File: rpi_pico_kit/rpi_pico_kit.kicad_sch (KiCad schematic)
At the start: 34 parts, among them J1 DC Jack 5.5x2.1mm, J3 Conn_01x03_Male, Q1 DMN63D8L-7, Q2 DMN63D8L-7, SW1 SW_Push, U1 RPi Pico, U5 74HC14

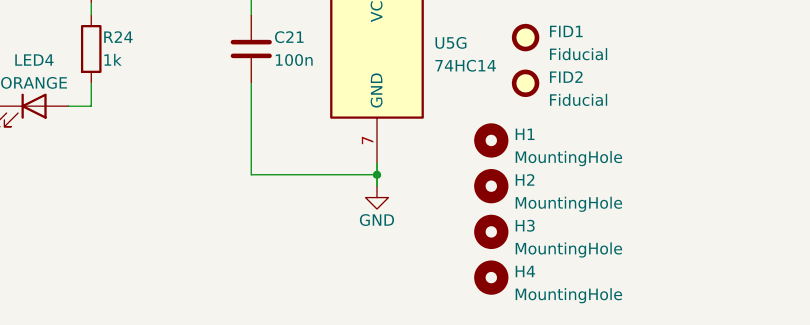
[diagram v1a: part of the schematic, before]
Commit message: added 5th hole at the center
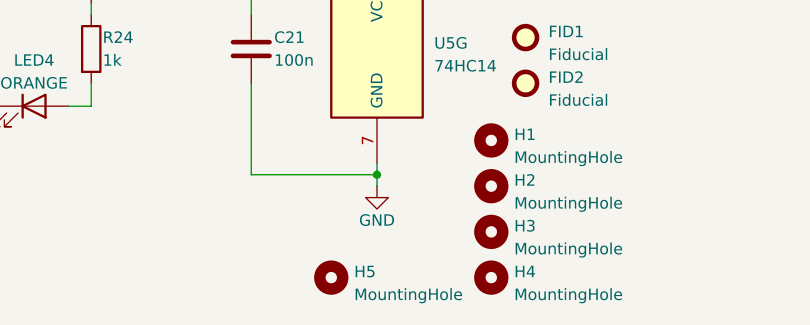
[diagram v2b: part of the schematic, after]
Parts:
- added H5: MountingHole, MountingHole:MountingHole_2.7mm_M2.5, symbol Mechanical:MountingHole
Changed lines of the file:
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@@
     (pin "2")
+  )
+  (symbol (lib_id "Mechanical:MountingHole") (at 142.24 194.31 0) (unit 1)
+    (in_bom yes) (on_board yes) (fields_autoplaced)
+    (property "Reference" "H5" (id 0) (at 144.78 193.675 0)
+      (effects (font (size 1.27 1.27)) (justify left))
+    )
+    (property "Value" "MountingHole" (id 1) (at 144.78 196.215 0)
+      (effects (font (size 1.27 1.27)) (justify left))
+    )
+    (property "Footprint" "MountingHole:MountingHole_2.7mm_M2.5" (id 2) (at 142.24 194.31 0)
+      (effects (font (size 1.27 1.27)) hide)
+    )
+    (property "Datasheet" "~" (id 3) (at 142.24 194.31 0)
+      (effects (font (size 1.27 1.27)) hide)
+    )
+    (property "Manufacturer Part Number" "~" (id 4) (at 142.24 194.31 0)
+      (effects (font (size 1.27 1.27)) hide)
+    )
+    (property "Supplier" "~" (id 5) (at 142.24 194.31 0)
+      (effects (font (size 1.27 1.27)) hide)
+    )
+    (property "Supplier Part URL" "~" (id 6) (at 142.24 194.31 0)
+      (effects (font (size 1.27 1.27)) hide)
+    )
   )
   (symbol (lib_id "power:GND") (at 85.09 158.75 0) (unit 1)
@@
       (reference "H4") (unit 1) (value "MountingHole") (footprint "MountingHole:MountingHole_2.7mm_M2.5")
     )
+    (path "/6a5cd9f1-fa39-4f86-88b6-0cd65263ec3f"
+      (reference "H5") (unit 1) (value "MountingHole") (footprint "MountingHole:MountingHole_2.7mm_M2.5")
+    )
     (path "/1be26fdf-4440-4eee-ae3b-ea83403c36c3"

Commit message: debugger (unrouted 163)
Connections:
- net +3V3: now also RN3.2 (R2.1), RN3.3 (R3.1); no longer RN3.1 (R1.1), RN3.2 (R2.1)
- net UART0_RX: now also RN3.7 (R2.2), RN3.8 (R1.2); no longer RN3.4 (R4.1), RN3.8 (R1.2)
- net UART0_TX: now also RN3.4 (R4.1); no longer RN3.3 (R3.1)
- net at U1.2 (GPIO1): now also RN3.1 (R1.1); no longer RN3.5 (R4.2)
- new net: RN3.5 (R4.2), RN3.6 (R3.2), U1.1 (GPIO0)
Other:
- moved on the sheet: RN3A
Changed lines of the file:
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@@
     (pin "1")
   )
-  (symbol (lib_id "Device:R_Pack04_Split") (at 44.45 36.83 270) (unit 4)
-    (in_bom yes) (on_board yes)
-    (property "Reference" "RN3" (id 0) (at 40.64 35.56 90)
+  (symbol (lib_id "Device:R_Pack04_Split") (at 44.45 36.83 90) (mirror x) (unit 1)
+    (in_bom yes) (on_board yes)
+    (property "Reference" "RN3" (id 0) (at 48.26 35.56 90)
       (effects (font (size 1.27 1.27)) (justify right))
     )
-    (property "Value" "1k" (id 1) (at 50.8 35.56 90)
+    (property "Value" "1k" (id 1) (at 38.1 35.56 90)
       (effects (font (size 1.27 1.27)) (justify right))
     )
@@
       (effects (font (size 1.27 1.27)) hide)
     )
-    (pin "4")
-    (pin "5")
+    (pin "1")
+    (pin "8")
   )
   (symbol (lib_id "power:GND") (at 140.97 62.23 0) (unit 1)
@@
     (pin "2")
   )
-  (symbol (lib_id "Device:R_Pack04_Split") (at 44.45 34.29 270) (unit 3)
+  (symbol (lib_id "Device:R_Pack04_Split") (at 44.45 34.29 270) (unit 4)
     (in_bom yes) (on_board yes)
     (property "Reference" "RN3" (id 0) (at 40.64 33.02 90)
@@
       (effects (font (size 1.27 1.27)) hide)
     )
-    (pin "3")
-    (pin "6")
+    (pin "4")
+    (pin "5")
   )
   (symbol (lib_id "Transistor_FET:BSS138") (at 144.78 101.6 270) (unit 1)
@@
     (pin "1")
   )
-  (symbol (lib_id "Device:R_Pack04_Split") (at 54.61 26.67 180) (unit 2)
+  (symbol (lib_id "Device:R_Pack04_Split") (at 54.61 26.67 180) (unit 3)
     (in_bom yes) (on_board yes)
     (property "Reference" "RN3" (id 0) (at 55.88 25.4 0)
@@
       (effects (font (size 1.27 1.27)) hide)
     )
-    (pin "2")
-    (pin "7")
+    (pin "3")
+    (pin "6")
   )
   (symbol (lib_id "power:GND") (at 196.85 151.13 90) (unit 1)
@@
     (pin "1")
   )
-  (symbol (lib_id "Device:R_Pack04_Split") (at 33.02 26.67 180) (unit 1)
+  (symbol (lib_id "Device:R_Pack04_Split") (at 33.02 26.67 180) (unit 2)
     (in_bom yes) (on_board yes)
     (property "Reference" "RN3" (id 0) (at 34.29 25.4 0)
@@
       (effects (font (size 1.27 1.27)) hide)
     )
-    (pin "1")
-    (pin "8")
+    (pin "2")
+    (pin "7")
   )
   (symbol (lib_id "Device:R") (at 115.57 140.97 0) (unit 1)
@@
       (reference "RN2") (unit 4) (value "270R") (footprint "Resistor_SMD:R_Array_Convex_4x0603")
     )
+    (path "/1ac4a7c2-b7be-4e1c-a497-ed6aab390c53"
+      (reference "RN3") (unit 1) (value "1k") (footprint "Resistor_SMD:R_Array_Convex_4x0603")
+    )
     (path "/d61b4a07-386e-408b-9033-b22a8b79e947"
-      (reference "RN3") (unit 1) (value "1k") (footprint "Resistor_SMD:R_Array_Convex_4x0603")
+      (reference "RN3") (unit 2) (value "1k") (footprint "Resistor_SMD:R_Array_Convex_4x0603")
     )
     (path "/cb5269f7-df36-404c-9295-80e9ad4fd32e"
-      (reference "RN3") (unit 2) (value "1k") (footprint "Resistor_SMD:R_Array_Convex_4x0603")
+      (reference "RN3") (unit 3) (value "1k") (footprint "Resistor_SMD:R_Array_Convex_4x0603")
     )
     (path "/5db5a00f-59fb-4bcf-a0f0-3bf8a625fc7d"
-      (reference "RN3") (unit 3) (value "1k") (footprint "Resistor_SMD:R_Array_Convex_4x0603")
-    )
-    (path "/1ac4a7c2-b7be-4e1c-a497-ed6aab390c53"
       (reference "RN3") (unit 4) (value "1k") (footprint "Resistor_SMD:R_Array_Convex_4x0603")
     )

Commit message: monostable (unrouted 136)
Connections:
- net UART0_RX: now also U5.3; no longer U5.5
- net at C19.2, R19.2, R20.1: now also U5.13; no longer U5.3
- net at LED3.1 (K): now also U5.12; no longer U5.4
- net at D5.2 (A): now also U5.4; no longer U5.6
- net at C20.2, R22.2, R23.1: now also U5.11; no longer U5.9
- net at LED4.1 (K): now also U5.10; no longer U5.8
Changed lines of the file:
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@@
     (pin "9")
   )
-  (symbol (lib_id "74xx:74HC14") (at 44.45 175.26 0) (unit 3)
+  (symbol (lib_id "74xx:74HC14") (at 44.45 175.26 0) (unit 2)
     (in_bom yes) (on_board yes) (fields_autoplaced)
     (property "Reference" "U5" (id 0) (at 44.45 167.64 0)
@@
       (effects (font (size 1.27 1.27)) hide)
     )
-    (pin "5")
-    (pin "6")
+    (pin "3")
+    (pin "4")
   )
   (symbol (lib_id "power:GND") (at 81.28 88.9 0) (unit 1)
@@
     (pin "1")
   )
-  (symbol (lib_id "74xx:74HC14") (at 95.25 175.26 0) (unit 4)
+  (symbol (lib_id "74xx:74HC14") (at 95.25 175.26 0) (unit 5)
     (in_bom yes) (on_board yes) (fields_autoplaced)
     (property "Reference" "U5" (id 0) (at 95.25 167.64 0)
@@
       (effects (font (size 1.27 1.27)) hide)
     )
-    (pin "8")
-    (pin "9")
+    (pin "10")
+    (pin "11")
   )
   (symbol (lib_id "power:GND") (at 74.93 158.75 0) (unit 1)
@@
     (pin "1")
   )
-  (symbol (lib_id "74xx:74HC14") (at 95.25 147.32 0) (unit 2)
+  (symbol (lib_id "74xx:74HC14") (at 95.25 147.32 0) (unit 6)
     (in_bom yes) (on_board yes) (fields_autoplaced)
     (property "Reference" "U5" (id 0) (at 95.25 139.7 0)
@@
       (effects (font (size 1.27 1.27)) hide)
     )
-    (pin "3")
-    (pin "4")
+    (pin "12")
+    (pin "13")
   )
   (symbol (lib_id "Device:R") (at 85.09 181.61 0) (unit 1)
@@
       (reference "U5") (unit 1) (value "74HC14") (footprint "Package_SO:SOIC-14_3.9x8.7mm_P1.27mm")
     )
+    (path "/919f662f-b70b-4993-9ea2-ad54dc351e72"
+      (reference "U5") (unit 2) (value "74HC14") (footprint "Package_SO:SOIC-14_3.9x8.7mm_P1.27mm")
+    )
+    (path "/fe15dc26-52fc-427e-8179-2b8bb41b57bb/f32a0f73-1820-4ea7-8063-dc0a550d2cec"
+      (reference "U5") (unit 3) (value "74HC14") (footprint "Package_SO:SOIC-14_3.9x8.7mm_P1.27mm")
+    )
+    (path "/fe15dc26-52fc-427e-8179-2b8bb41b57bb/bbbac723-7fcc-4a53-b5f6-de5daa58086a"
+      (reference "U5") (unit 4) (value "74HC14") (footprint "Package_SO:SOIC-14_3.9x8.7mm_P1.27mm")
+    )
+    (path "/d2118661-349f-4f17-a649-7ecad9caafc3"
+      (reference "U5") (unit 5) (value "74HC14") (footprint "Package_SO:SOIC-14_3.9x8.7mm_P1.27mm")
+    )
     (path "/f6bee219-67fb-464f-b724-02f155dc53f3"
-      (reference "U5") (unit 2) (value "74HC14") (footprint "Package_SO:SOIC-14_3.9x8.7mm_P1.27mm")
-    )
-    (path "/919f662f-b70b-4993-9ea2-ad54dc351e72"
-      (reference "U5") (unit 3) (value "74HC14") (footprint "Package_SO:SOIC-14_3.9x8.7mm_P1.27mm")
-    )
-    (path "/d2118661-349f-4f17-a649-7ecad9caafc3"
-      (reference "U5") (unit 4) (value "74HC14") (footprint "Package_SO:SOIC-14_3.9x8.7mm_P1.27mm")
-    )
-    (path "/fe15dc26-52fc-427e-8179-2b8bb41b57bb/f32a0f73-1820-4ea7-8063-dc0a550d2cec"
-      (reference "U5") (unit 5) (value "74HC14") (footprint "Package_SO:SOIC-14_3.9x8.7mm_P1.27mm")
-    )
-    (path "/fe15dc26-52fc-427e-8179-2b8bb41b57bb/bbbac723-7fcc-4a53-b5f6-de5daa58086a"
       (reference "U5") (unit 6) (value "74HC14") (footprint "Package_SO:SOIC-14_3.9x8.7mm_P1.27mm")
     )

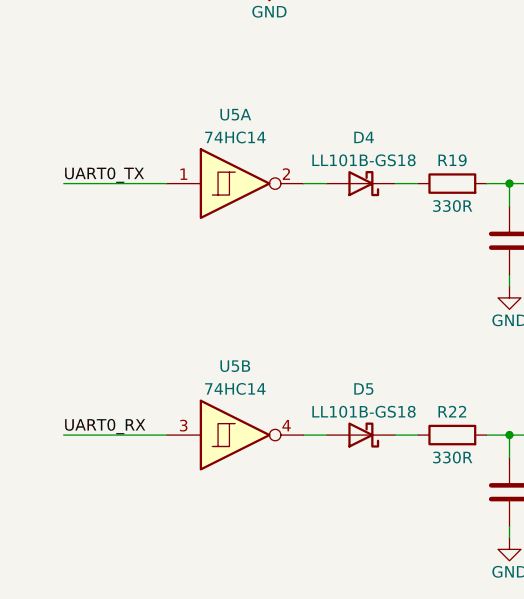
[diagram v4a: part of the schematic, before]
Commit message: changed pinout
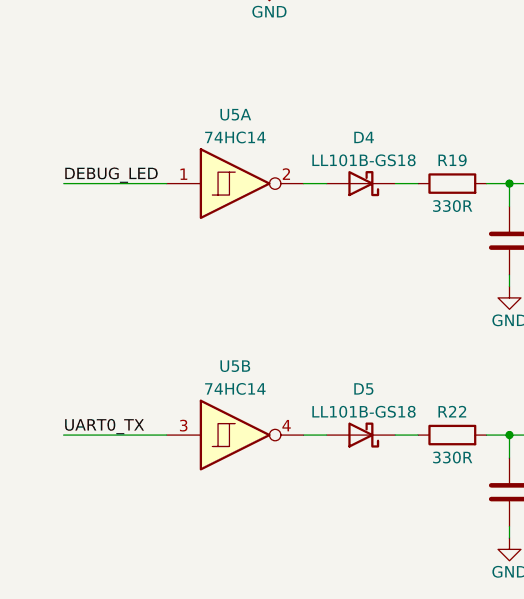
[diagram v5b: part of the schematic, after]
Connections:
- net UART0_RX: no longer U5.3
- net UART0_TX: now also U5.3; no longer U5.1
- new net DEBUG_LED: U5.1
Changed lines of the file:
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@@
     (effects (font (size 1.27 1.27)) (justify right bottom))
   )
-  (label "UART0_RX" (at 25.4 175.26 0) (fields_autoplaced)
+  (label "UART0_TX" (at 25.4 175.26 0) (fields_autoplaced)
     (effects (font (size 1.27 1.27)) (justify left bottom))
   )
@@
     (effects (font (size 1.27 1.27)) (justify left bottom))
   )
-  (label "UART0_TX" (at 25.4 147.32 0) (fields_autoplaced)
+  (label "DEBUG_LED" (at 25.4 147.32 0) (fields_autoplaced)
     (effects (font (size 1.27 1.27)) (justify left bottom))
   )

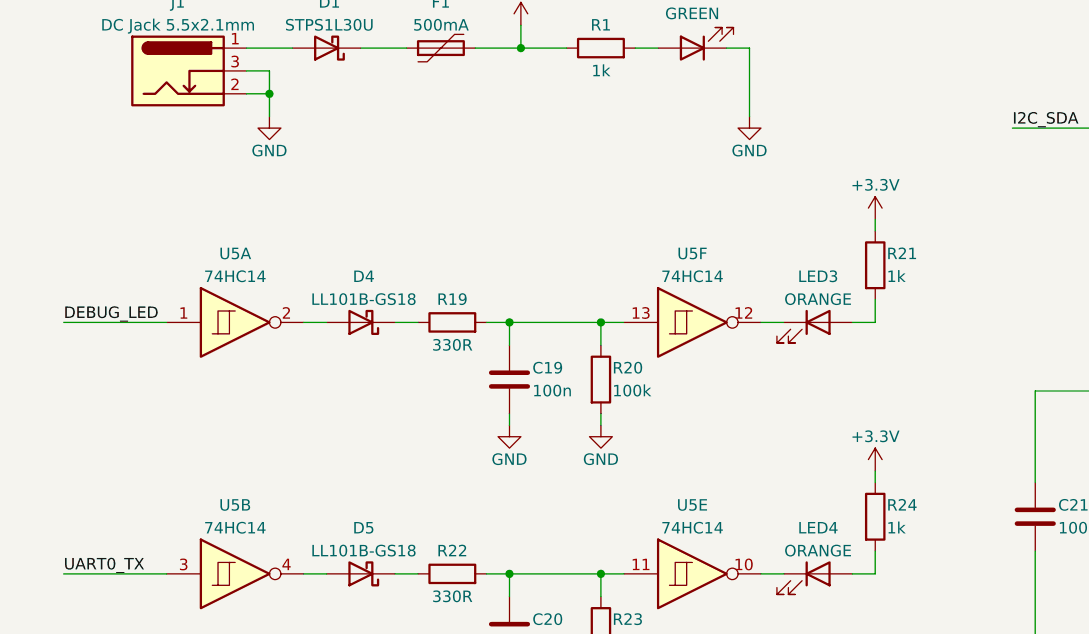
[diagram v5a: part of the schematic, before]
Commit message: changed pinout
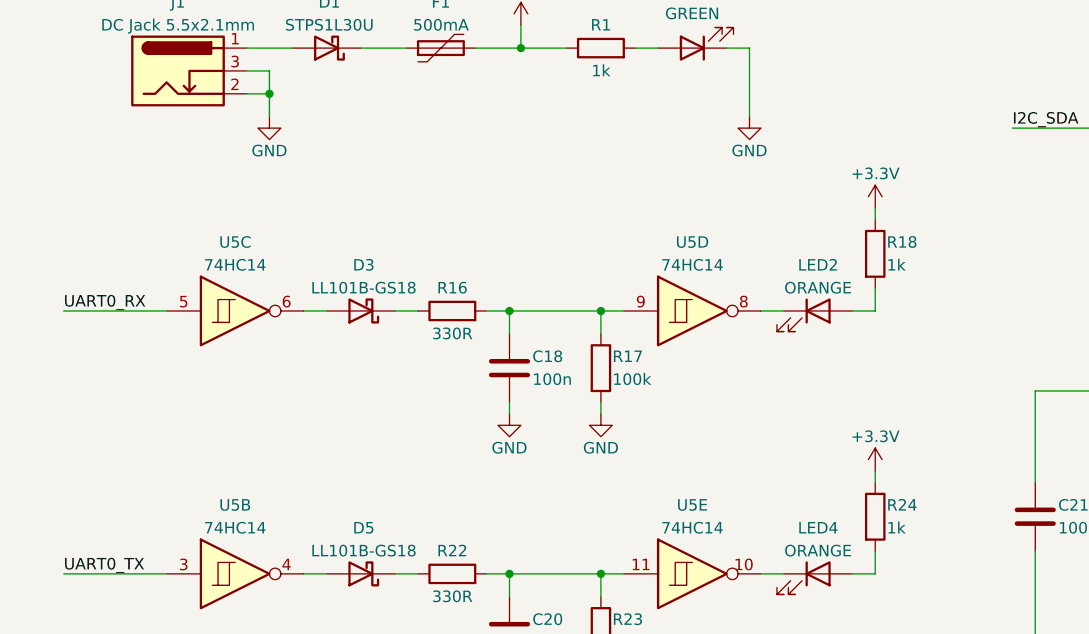
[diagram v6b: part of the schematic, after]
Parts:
- removed C19: 100n, Capacitor_SMD:C_0603_1608Metric_Pad1.08x0.95mm_HandSolder, symbol Device:C
- removed D4: LL101B-GS18, Diode_SMD:D_MiniMELF, symbol Device:D_Schottky
- removed LED3: ORANGE, LED_SMD:LED_0805_2012Metric_Pad1.15x1.40mm_HandSolder, symbol Device:LED
- removed R19: 330R, Resistor_SMD:R_0603_1608Metric_Pad0.98x0.95mm_HandSolder, symbol Device:R
- removed R20: 100k, Resistor_SMD:R_0603_1608Metric_Pad0.98x0.95mm_HandSolder, symbol Device:R
- removed R21: 1k, Resistor_SMD:R_0603_1608Metric_Pad0.98x0.95mm_HandSolder, symbol Device:R
- removed unit 1 of U5
- removed unit 6 of U5
- added C18: 100n, Capacitor_SMD:C_0603_1608Metric_Pad1.08x0.95mm_HandSolder, symbol Device:C
- added D3: LL101B-GS18, Diode_SMD:D_MiniMELF, symbol Device:D_Schottky
- added LED2: ORANGE, LED_SMD:LED_0805_2012Metric_Pad1.15x1.40mm_HandSolder, symbol Device:LED
- added R16: 330R, Resistor_SMD:R_0603_1608Metric_Pad0.98x0.95mm_HandSolder, symbol Device:R
- added R17: 100k, Resistor_SMD:R_0603_1608Metric_Pad0.98x0.95mm_HandSolder, symbol Device:R
- added R18: 1k, Resistor_SMD:R_0603_1608Metric_Pad0.98x0.95mm_HandSolder, symbol Device:R
- added unit 3 of U5
- added unit 4 of U5
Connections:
- net +3V3: now also R18.1
- net GND: now also C18.1, R17.2
- net UART0_RX: now also U5.5
- new net: D3.1 (K), R16.1
- new net: C18.2, R16.2, R17.1, U5.9
- new net: D3.2 (A), U5.6
- new net: LED2.1 (K), U5.8
- new net: LED2.2 (A), R18.2

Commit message: fiducials
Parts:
- added FID3: Fiducial, Fiducial:Fiducial_0.75mm_Mask1.5mm, symbol Mechanical:Fiducial
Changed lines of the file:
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@@
     (pin "2")
+  )
+  (symbol (lib_id "Mechanical:Fiducial") (at 163.83 162.56 0) (unit 1)
+    (in_bom yes) (on_board yes) (fields_autoplaced)
+    (property "Reference" "FID3" (id 0) (at 166.37 161.925 0)
+      (effects (font (size 1.27 1.27)) (justify left))
+    )
+    (property "Value" "Fiducial" (id 1) (at 166.37 164.465 0)
+      (effects (font (size 1.27 1.27)) (justify left))
+    )
+    (property "Footprint" "Fiducial:Fiducial_0.75mm_Mask1.5mm" (id 2) (at 163.83 162.56 0)
+      (effects (font (size 1.27 1.27)) hide)
+    )
+    (property "Datasheet" "~" (id 3) (at 163.83 162.56 0)
+      (effects (font (size 1.27 1.27)) hide)
+    )
+    (property "Manufacturer Part Number" "~" (id 4) (at 163.83 162.56 0)
+      (effects (font (size 1.27 1.27)) hide)
+    )
+    (property "Supplier" "~" (id 5) (at 163.83 162.56 0)
+      (effects (font (size 1.27 1.27)) hide)
+    )
+    (property "Supplier Part URL" "~" (id 6) (at 163.83 162.56 0)
+      (effects (font (size 1.27 1.27)) hide)
+    )
   )
   (symbol (lib_id "power:GND") (at 85.09 186.69 0) (unit 1)
@@
       (reference "FID2") (unit 1) (value "Fiducial") (footprint "Fiducial:Fiducial_0.75mm_Mask1.5mm")
     )
+    (path "/ba288efc-18e4-4aa1-a487-ba1da00306a7"
+      (reference "FID3") (unit 1) (value "Fiducial") (footprint "Fiducial:Fiducial_0.75mm_Mask1.5mm")
+    )
     (path "/2742ad94-0e2b-4aaf-bb30-f67347c61c2a"
